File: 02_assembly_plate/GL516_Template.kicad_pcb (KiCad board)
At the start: 2 copper layers, 314.4 x 98.8 mm, 58 parts, among them J10 Conn_01x01, J11 Conn_01x01, J12 Conn_01x01, J13 Conn_01x01, J14 Conn_01x01, J15 Conn_01x01, J16 Conn_01x01, J17 Conn_01x01, J2 Conn_01x01, J3 Conn_01x01, J4 Conn_01x01, J5 Conn_01x01, J6 Conn_01x01, J7 Conn_01x01, J8 Conn_01x01, J9 Conn_01x01, SW1 KEY_SWITCH, SW10 KEY_SWITCH, SW11 KEY_SWITCH, SW12 KEY_SWITCH, SW13 KEY_SWITCH, SW14 KEY_SWITCH, SW15 KEY_SWITCH, SW16 KEY_SWITCH, SW17 KEY_SWITCH, SW18 KEY_SWITCH, SW19 KEY_SWITCH, SW2 KEY_SWITCH, SW20 KEY_SWITCH, SW21 KEY_SWITCH, SW22 KEY_SWITCH, SW23 KEY_SWITCH, SW24 KEY_SWITCH, SW25 KEY_SWITCH, SW26 KEY_SWITCH, SW27 KEY_SWITCH, SW28 KEY_SWITCH, SW29 KEY_SWITCH, SW3 KEY_SWITCH, SW30 KEY_SWITCH, SW31 KEY_SWITCH, SW32 KEY_SWITCH, SW33 KEY_SWITCH, SW34 KEY_SWITCH, SW35 KEY_SWITCH, SW36 KEY_SWITCH, SW37 KEY_SWITCH, SW38 KEY_SWITCH, SW39 KEY_SWITCH, SW4 KEY_SWITCH, SW40 KEY_SWITCH, SW41 KEY_SWITCH, SW42 KEY_SWITCH, SW5 KEY_SWITCH, SW6 KEY_SWITCH, SW7 KEY_SWITCH, SW8 KEY_SWITCH, SW9 KEY_SWITCH

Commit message: place all footprints and change edge.cuts
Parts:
- removed J10, J11, J12, J13, J14, J15, J16, J17, J8, J9: Conn_01x01, kbd_Hole:m2_Screw_Hole_Fab
- removed J2, J3, J4, J5, J6, J7: Conn_01x01, kbd_Hole:m2_Screw_Hole_EdgeCuts
- added D1: D, kbd_Parts:Diode_TH_SMD, F.Cu at (36.1, 53.3)
- added D10: D, kbd_Parts:Diode_TH_SMD, F.Cu at (93.3, 53.3)
- added D11: D, kbd_Parts:Diode_TH_SMD, F.Cu at (93.3, 72.3)
- added D12: D, kbd_Parts:Diode_TH_SMD, F.Cu at (93.3, 91.4)
- added D13: D, kbd_Parts:Diode_TH_SMD, F.Cu at (112.3, 53.3)
- added D14: D, kbd_Parts:Diode_TH_SMD, F.Cu at (112.3, 72.3)
- added D15: D, kbd_Parts:Diode_TH_SMD, F.Cu at (112.3, 91.4)
- added D16: D, kbd_Parts:Diode_TH_SMD, F.Cu at (112.3, 110.4)
- added D17: D, kbd_Parts:Diode_TH_SMD, F.Cu at (131.4, 53.3)
- added D18: D, kbd_Parts:Diode_TH_SMD, F.Cu at (131.4, 72.3)
- added D19: D, kbd_Parts:Diode_TH_SMD, F.Cu at (131.4, 91.4)
- added D2: D, kbd_Parts:Diode_TH_SMD, F.Cu at (36.1, 72.3)
- added D20: D, kbd_Parts:Diode_TH_SMD, F.Cu at (131.4, 110.4)
- added D21: D, kbd_Parts:Diode_TH_SMD, F.Cu at (150.4, 110.4)
- added D22: D, kbd_Parts:Diode_TH_SMD, F.Cu at (207.6, 110.4)
- added D23: D, kbd_Parts:Diode_TH_SMD, F.Cu at (226.6, 53.3)
- added D24: D, kbd_Parts:Diode_TH_SMD, F.Cu at (226.6, 72.3)
- added D25: D, kbd_Parts:Diode_TH_SMD, F.Cu at (226.6, 91.4)
- added D26: D, kbd_Parts:Diode_TH_SMD, F.Cu at (226.6, 110.4)
- added D27: D, kbd_Parts:Diode_TH_SMD, F.Cu at (245.7, 53.3)
- added D28: D, kbd_Parts:Diode_TH_SMD, F.Cu at (245.7, 72.3)
- added D29: D, kbd_Parts:Diode_TH_SMD, F.Cu at (245.7, 91.4)
- added D3: D, kbd_Parts:Diode_TH_SMD, F.Cu at (36.1, 91.4)
- added D30: D, kbd_Parts:Diode_TH_SMD, F.Cu at (245.7, 110.4)
- added D31: D, kbd_Parts:Diode_TH_SMD, F.Cu at (264.7, 53.3)
- added D32: D, kbd_Parts:Diode_TH_SMD, F.Cu at (264.7, 72.3)
- added D33: D, kbd_Parts:Diode_TH_SMD, F.Cu at (264.7, 91.4)
- added D34: D, kbd_Parts:Diode_TH_SMD, F.Cu at (283.8, 53.3)
- added D35: D, kbd_Parts:Diode_TH_SMD, F.Cu at (283.8, 72.3)
- added D36: D, kbd_Parts:Diode_TH_SMD, F.Cu at (283.8, 91.4)
- added D37: D, kbd_Parts:Diode_TH_SMD, F.Cu at (302.8, 53.3)
- added D38: D, kbd_Parts:Diode_TH_SMD, F.Cu at (302.8, 72.3)
- added D39: D, kbd_Parts:Diode_TH_SMD, F.Cu at (302.8, 91.4)
- added D4: D, kbd_Parts:Diode_TH_SMD, F.Cu at (55.2, 53.3)
- added D40: D, kbd_Parts:Diode_TH_SMD, F.Cu at (321.9, 53.3)
- added D41: D, kbd_Parts:Diode_TH_SMD, F.Cu at (321.9, 72.3)
- added D42: D, kbd_Parts:Diode_TH_SMD, F.Cu at (321.9, 91.4)
- added D5: D, kbd_Parts:Diode_TH_SMD, F.Cu at (55.2, 72.3)
- added D6: D, kbd_Parts:Diode_TH_SMD, F.Cu at (55.2, 91.4)
- added D7: D, kbd_Parts:Diode_TH_SMD, F.Cu at (74.2, 53.3)
- added D8: D, kbd_Parts:Diode_TH_SMD, F.Cu at (74.2, 72.3)
- added D9: D, kbd_Parts:Diode_TH_SMD, F.Cu at (74.2, 91.4)
- added J1: Conn_01x02, kbd_Parts:Battery_XH2.5_GL_PCB, F.Cu at (254.9, 23.8)
- added SW43: SW_PUSH, kbd_Parts:ResetSW, F.Cu at (271.4, 21.4)
- added U1: BLEMicroPro, kbd_Parts:Micon_BMP_GL, B.Cu at (301.6, 28.5)
- SW1, SW10, SW11, SW12, SW13, SW14, SW15, SW16, SW17, SW18, SW19, SW2, SW20, SW21, SW22, SW23, SW24, SW25, SW26, SW27, SW28, SW29, SW3, SW30, SW31, SW32, SW33, SW34, SW35, SW36, SW37, SW38, SW39, SW4, SW40, SW41, SW42, SW5, SW6, SW7, SW8, SW9: value KEY_SWITCH -> SW_PUSH; footprint kbd_SW_Hole:SW_Hole_1 -> kbd_SW:CherryMX_Hotswap_1.0u
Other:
- board size 314.4 x 98.8 mm -> 304.4 x 98.8 mm
- board text removed: "Put the ProMicro between here and there."

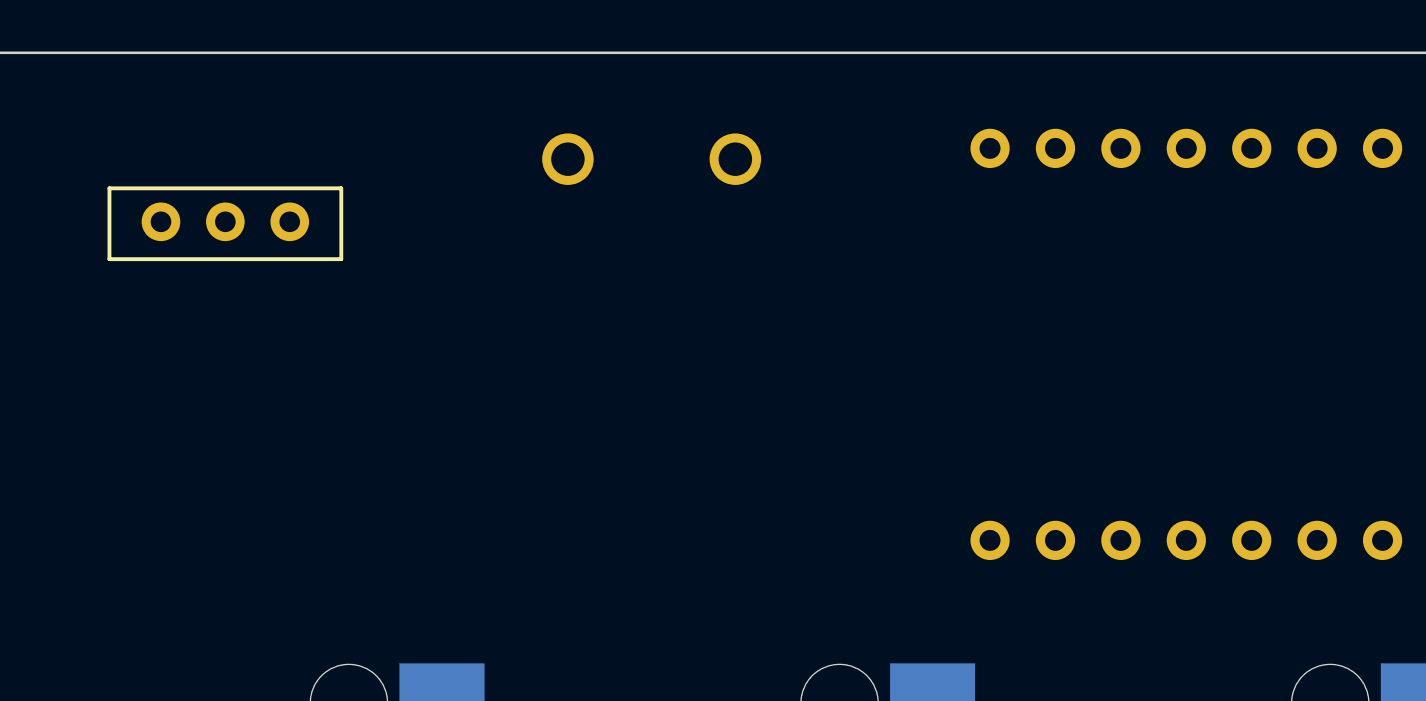
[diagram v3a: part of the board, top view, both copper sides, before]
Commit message: Wire GND, RST, BAT+
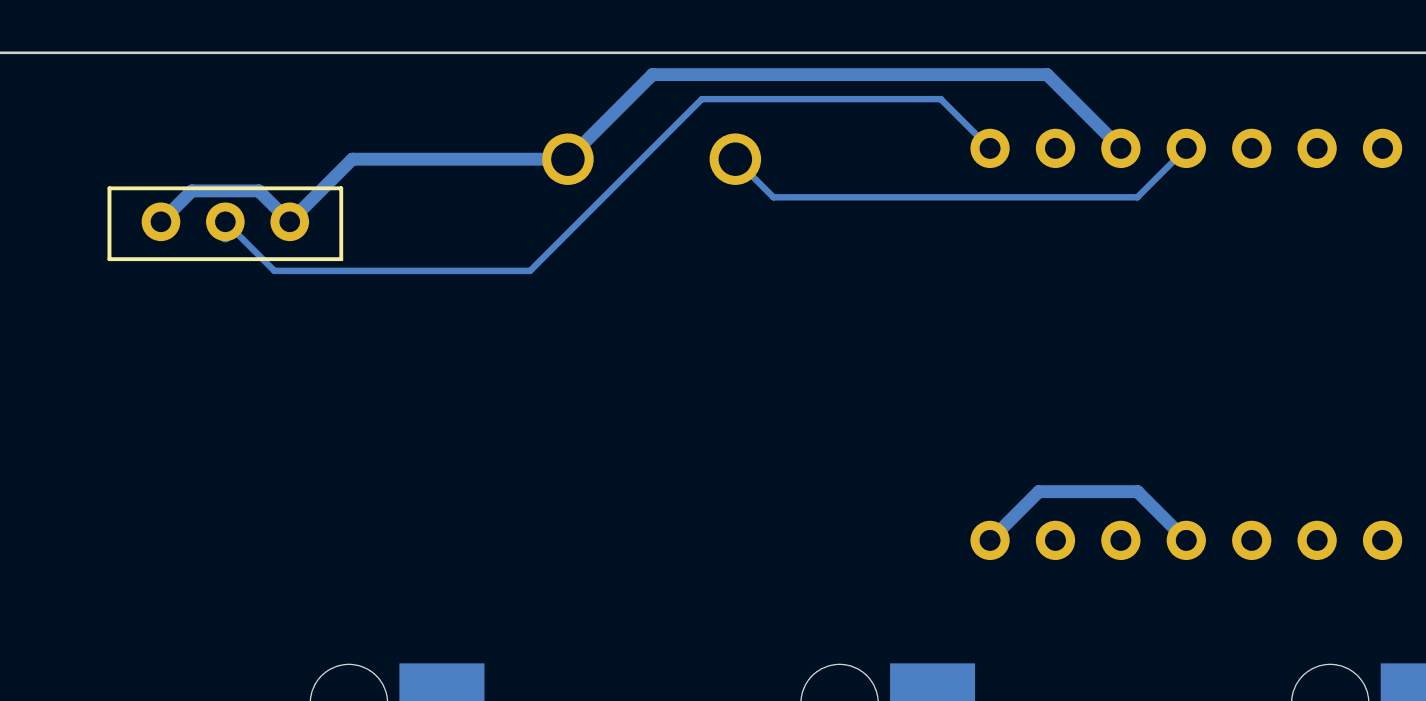
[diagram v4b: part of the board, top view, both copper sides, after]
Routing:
- net GND: track 0.00 -> 51.2 mm
- net Bat+: track 0.00 -> 34.8 mm
- net Reset: track 0.00 -> 18.9 mm
- net VCC: track 0.00 -> 0.53 mm
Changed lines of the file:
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@@
     (thickness 1.6)
     (drawings 701)
-    (tracks 0)
+    (tracks 24)
     (zones 0)
     (modules 87)
@@
     (38 B.Mask user)
     (39 F.Mask user)
-    (40 Dwgs.User user)
+    (40 Dwgs.User user hide)
     (41 Cmts.User user)
     (42 Eco1.User user)
@@
     (solder_mask_min_width 0.25)
     (aux_axis_origin 0 0)
-    (grid_origin 28.525 47.575)
     (visible_elements 7FFFFFFF)
     (pcbplotparams
@@
       (effects (font (size 0.75 0.5) (thickness 0.125)) (justify mirror))
     )
-    (fp_text user LED (at 5.5 14.478 270) (layer B.SilkS)
+    (fp_text user " " (at 5.5 14.478 270) (layer B.SilkS)
       (effects (font (size 0.75 0.5) (thickness 0.125)) (justify mirror))
     )
@@
   (gr_line (start 22.275 116.05) (end 320.625 116.05) (layer Edge.Cuts) (width 0.1))
   (gr_line (start 320.625 17.25) (end 22.275 17.25) (layer Edge.Cuts) (width 0.1))
+  (segment (start 259.7985 21.3807) (end 257.3672 23.812) (width 0.5) (layer B.Cu) (net 47))
+  (segment (start 268.1676 21.3807) (end 259.7985 21.3807) (width 0.5) (layer B.Cu) (net 47))
+  (segment (start 253.567201 22.611999) (end 252.3672 23.812) (width 0.5) (layer B.Cu) (net 47))
+  (segment (start 256.167199 22.611999) (end 253.567201 22.611999) (width 0.5) (layer B.Cu) (net 47))
+  (segment (start 257.3672 23.812) (end 256.167199 22.611999) (width 0.5) (layer B.Cu) (net 47))
+  (segment (start 284.7839 36.1814) (end 284.557 36.1814) (width 0.5) (layer B.Cu) (net 47))
+  (segment (start 290.2856 34.29) (end 292.177 36.1814) (width 0.5) (layer B.Cu) (net 47))
+  (segment (start 286.4484 34.29) (end 290.2856 34.29) (width 0.5) (layer B.Cu) (net 47))
+  (segment (start 284.557 36.1814) (end 286.4484 34.29) (width 0.5) (layer B.Cu) (net 47))
+  (segment (start 271.4508 18.0975) (end 268.1676 21.3807) (width 0.5) (layer B.Cu) (net 47))
+  (segment (start 286.7731 18.0975) (end 271.4508 18.0975) (width 0.5) (layer B.Cu) (net 47))
+  (segment (start 289.637 20.9614) (end 286.7731 18.0975) (width 0.5) (layer B.Cu) (net 47))
+  (segment (start 254.8672 24.3622) (end 254.8672 23.812) (width 0.5) (layer B.Cu) (net 48))
+  (segment (start 284.7911 20.9614) (end 284.557 20.9614) (width 0.5) (layer B.Cu) (net 48))
+  (segment (start 266.7 25.7175) (end 256.7727 25.7175) (width 0.25) (layer B.Cu) (net 48))
+  (segment (start 273.3675 19.05) (end 266.7 25.7175) (width 0.25) (layer B.Cu) (net 48))
+  (segment (start 256.7727 25.7175) (end 254.8672 23.812) (width 0.25) (layer B.Cu) (net 48))
+  (segment (start 282.6456 19.05) (end 273.3675 19.05) (width 0.25) (layer B.Cu) (net 48))
+  (segment (start 284.557 20.9614) (end 282.6456 19.05) (width 0.25) (layer B.Cu) (net 48))
+  (segment (start 276.1469 22.86) (end 274.6676 21.3807) (width 0.25) (layer B.Cu) (net 56))
+  (segment (start 290.2784 22.86) (end 276.1469 22.86) (width 0.25) (layer B.Cu) (net 56))
+  (segment (start 292.177 20.9614) (end 290.2784 22.86) (width 0.25) (layer B.Cu) (net 56))
+  (segment (start 294.717 20.9614) (end 295.1686 20.9614) (width 0.5) (layer B.Cu) (net 64))
+  (segment (start 295.1686 20.9614) (end 295.225 20.905) (width 0.5) (layer B.Cu) (net 64))
 )

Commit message: Wire Diode's PAT and Pin Hole
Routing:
- net Row0: track 0.00 -> 24.5 mm
- net Row2: track 0.00 -> 24.4 mm
- net Row1: track 0.00 -> 22.4 mm
- net Row3: track 0.00 -> 12.3 mm
- net Net-(D30-Pad1): track 0.00 -> 2.04 mm
- net Net-(D26-Pad1): track 0.00 -> 2.04 mm
- net Net-(D22-Pad1): track 0.00 -> 2.04 mm
- net Net-(D21-Pad2): track 0.00 -> 2.04 mm
- net Net-(D20-Pad2): track 0.00 -> 2.04 mm
- net Net-(D16-Pad2): track 0.00 -> 2.04 mm
- net Net-(D7-Pad2): track 0.00 -> 2.04 mm
- net Net-(D40-Pad1): track 0.00 -> 2.04 mm
- net Net-(D4-Pad2): track 0.00 -> 2.04 mm
- net Net-(D37-Pad1): track 0.00 -> 2.04 mm
- net Net-(D34-Pad1): track 0.00 -> 2.04 mm
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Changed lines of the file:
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@@
     (thickness 1.6)
     (drawings 701)
-    (tracks 24)
+    (tracks 110)
     (zones 0)
     (modules 87)
@@
   (page A3)
   (layers
-    (0 F.Cu signal)
+    (0 F.Cu signal hide)
     (31 B.Cu signal)
-    (32 B.Adhes user)
-    (33 F.Adhes user)
+    (32 B.Adhes user hide)
+    (33 F.Adhes user hide)
     (34 B.Paste user)
-    (35 F.Paste user)
-    (36 B.SilkS user)
-    (37 F.SilkS user)
+    (35 F.Paste user hide)
+    (36 B.SilkS user hide)
+    (37 F.SilkS user hide)
     (38 B.Mask user)
-    (39 F.Mask user)
+    (39 F.Mask user hide)
     (40 Dwgs.User user hide)
-    (41 Cmts.User user)
-    (42 Eco1.User user)
-    (43 Eco2.User user)
+    (41 Cmts.User user hide)
+    (42 Eco1.User user hide)
+    (43 Eco2.User user hide)
     (44 Edge.Cuts user)
-    (45 Margin user)
+    (45 Margin user hide)
     (46 B.CrtYd user)
-    (47 F.CrtYd user)
+    (47 F.CrtYd user hide)
     (48 B.Fab user)
-    (49 F.Fab user)
+    (49 F.Fab user hide)
   )
   (setup
@@
     (solder_mask_min_width 0.25)
     (aux_axis_origin 0 0)
-    (visible_elements 7FFFFFFF)
+    (visible_elements 7FFFF7FF)
     (pcbplotparams
       (layerselection 0x01000_7ffffffe)
@@
   (gr_line (start 22.275 116.05) (end 320.625 116.05) (layer Edge.Cuts) (width 0.1))
   (gr_line (start 320.625 17.25) (end 22.275 17.25) (layer Edge.Cuts) (width 0.1))
+  (segment (start 36.145 49.48) (end 36.145 51.515) (width 0.25) (layer B.Cu) (net 1))
+  (segment (start 297.1936 36.1814) (end 297.257 36.1814) (width 0.25) (layer B.Cu) (net 2))
+  (segment (start 321.895 55.065) (end 321.895 57.1) (width 0.25) (layer B.Cu) (net 2))
+  (segment (start 302.845 55.065) (end 302.845 57.1) (width 0.25) (layer B.Cu) (net 2))
+  (segment (start 283.795 55.065) (end 283.795 57.1) (width 0.25) (layer B.Cu) (net 2))
+  (segment (start 264.745 55.065) (end 264.745 57.1) (width 0.25) (layer B.Cu) (net 2))
+  (segment (start 245.695 55.065) (end 245.695 57.1) (width 0.25) (layer B.Cu) (net 2))
+  (segment (start 226.645 55.065) (end 226.645 57.1) (width 0.25) (layer B.Cu) (net 2))
+  (segment (start 131.395 55.065) (end 131.395 57.1) (width 0.25) (layer B.Cu) (net 2))
+  (segment (start 112.345 55.065) (end 112.345 57.1) (width 0.25) (layer B.Cu) (net 2))
+  (segment (start 93.295 55.065) (end 93.295 57.1) (width 0.25) (layer B.Cu) (net 2))
+  (segment (start 74.245 55.065) (end 74.245 57.1) (width 0.25) (layer B.Cu) (net 2))
+  (segment (start 55.195 55.065) (end 55.195 57.1) (width 0.25) (layer B.Cu) (net 2))
+  (segment (start 36.145 55.065) (end 36.145 57.1) (width 0.25) (layer B.Cu) (net 2))
+  (segment (start 36.145 68.53) (end 36.145 70.565) (width 0.25) (layer B.Cu) (net 3))
+  (segment (start 321.895 74.115) (end 321.895 76.15) (width 0.25) (layer B.Cu) (net 4))
+  (segment (start 302.845 74.115) (end 302.845 76.15) (width 0.25) (layer B.Cu) (net 4))
+  (segment (start 283.795 74.115) (end 283.795 76.15) (width 0.25) (layer B.Cu) (net 4))
+  (segment (start 264.745 74.115) (end 264.745 76.15) (width 0.25) (layer B.Cu) (net 4))
+  (segment (start 245.695 74.115) (end 245.695 76.15) (width 0.25) (layer B.Cu) (net 4))
+  (segment (start 131.395 74.115) (end 131.395 76.15) (width 0.25) (layer B.Cu) (net 4))
+  (segment (start 112.345 74.115) (end 112.345 76.15) (width 0.25) (layer B.Cu) (net 4))
+  (segment (start 93.295 74.115) (end 93.295 76.15) (width 0.25) (layer B.Cu) (net 4))
+  (segment (start 74.245 74.115) (end 74.245 76.15) (width 0.25) (layer B.Cu) (net 4))
+  (segment (start 55.195 74.115) (end 55.195 76.15) (width 0.25) (layer B.Cu) (net 4))
+  (segment (start 36.145 74.115) (end 36.145 76.15) (width 0.25) (layer B.Cu) (net 4))
+  (segment (start 36.145 87.58) (end 36.145 89.615) (width 0.25) (layer B.Cu) (net 5))
+  (segment (start 302.337 36.1814) (end 302.3506 36.195) (width 0.25) (layer B.Cu) (net 6))
+  (segment (start 321.895 93.165) (end 321.895 95.2) (width 0.25) (layer B.Cu) (net 6))
+  (segment (start 302.845 93.165) (end 302.845 95.2) (width 0.25) (layer B.Cu) (net 6))
+  (segment (start 283.795 93.165) (end 283.795 95.2) (width 0.25) (layer B.Cu) (net 6))
+  (segment (start 264.745 93.165) (end 264.745 95.2) (width 0.25) (layer B.Cu) (net 6))
+  (segment (start 245.695 93.165) (end 245.695 95.2) (width 0.25) (layer B.Cu) (net 6))
+  (segment (start 226.645 93.165) (end 226.645 95.2) (width 0.25) (layer B.Cu) (net 6))
+  (segment (start 131.395 93.165) (end 131.395 95.2) (width 0.25) (layer B.Cu) (net 6))
+  (segment (start 112.345 93.165) (end 112.345 95.2) (width 0.25) (layer B.Cu) (net 6))
+  (segment (start 93.295 93.165) (end 93.295 95.2) (width 0.25) (layer B.Cu) (net 6))
+  (segment (start 74.245 93.165) (end 74.245 95.2) (width 0.25) (layer B.Cu) (net 6))
+  (segment (start 55.195 93.165) (end 55.195 95.2) (width 0.25) (layer B.Cu) (net 6))
+  (segment (start 36.145 93.165) (end 36.145 95.2) (width 0.25) (layer B.Cu) (net 6))
+  (segment (start 55.195 49.48) (end 55.195 51.515) (width 0.25) (layer B.Cu) (net 7))
+  (segment (start 55.195 68.53) (end 55.195 70.565) (width 0.25) (layer B.Cu) (net 8))
+  (segment (start 55.195 87.58) (end 55.195 89.615) (width 0.25) (layer B.Cu) (net 9))
+  (segment (start 74.245 49.48) (end 74.245 51.515) (width 0.25) (layer B.Cu) (net 10))
+  (segment (start 74.245 68.53) (end 74.245 70.565) (width 0.25) (layer B.Cu) (net 11))
+  (segment (start 93.295 49.48) (end 93.295 51.515) (width 0.25) (layer B.Cu) (net 13))
+  (segment (start 93.295 68.53) (end 93.295 70.565) (width 0.25) (layer B.Cu) (net 14))
+  (segment (start 93.295 87.58) (end 93.295 89.615) (width 0.25) (layer B.Cu) (net 15))
+  (segment (start 112.345 49.48) (end 112.345 51.515) (width 0.25) (layer B.Cu) (net 16))
+  (segment (start 112.345 68.53) (end 112.345 70.565) (width 0.25) (layer B.Cu) (net 17))
+  (segment (start 112.345 87.58) (end 112.345 89.615) (width 0.25) (layer B.Cu) (net 18))
+  (segment (start 112.345 106.63) (end 112.345 108.665) (width 0.25) (layer B.Cu) (net 19))
+  (segment (start 304.8136 36.1814) (end 304.877 36.1814) (width 0.25) (layer B.Cu) (net 20))
+  (segment (start 245.695 112.215) (end 245.695 114.25) (width 0.25) (layer B.Cu) (net 20))
+  (segment (start 226.645 112.215) (end 226.645 114.25) (width 0.25) (layer B.Cu) (net 20))
+  (segment (start 207.595 112.215) (end 207.595 114.25) (width 0.25) (layer B.Cu) (net 20))
+  (segment (start 150.445 112.215) (end 150.445 114.25) (width 0.25) (layer B.Cu) (net 20))
+  (segment (start 131.395 112.215) (end 131.395 114.25) (width 0.25) (layer B.Cu) (net 20))
+  (segment (start 112.345 112.215) (end 112.345 114.25) (width 0.25) (layer B.Cu) (net 20))
+  (segment (start 131.395 49.48) (end 131.395 51.515) (width 0.25) (layer B.Cu) (net 21))
+  (segment (start 131.395 68.53) (end 131.395 70.565) (width 0.25) (layer B.Cu) (net 22))
+  (segment (start 131.395 87.58) (end 131.395 89.615) (width 0.25) (layer B.Cu) (net 23))
+  (segment (start 131.395 106.63) (end 131.395 108.665) (width 0.25) (layer B.Cu) (net 24))
+  (segment (start 150.445 106.63) (end 150.445 108.665) (width 0.25) (layer B.Cu) (net 25))
+  (segment (start 207.595 106.63) (end 207.595 108.665) (width 0.25) (layer B.Cu) (net 26))
+  (segment (start 226.645 49.48) (end 226.645 51.515) (width 0.25) (layer B.Cu) (net 27))
+  (segment (start 226.645 68.53) (end 226.645 70.565) (width 0.25) (layer B.Cu) (net 28))
+  (segment (start 226.645 87.58) (end 226.645 89.615) (width 0.25) (layer B.Cu) (net 29))
+  (segment (start 226.645 106.63) (end 226.645 108.665) (width 0.25) (layer B.Cu) (net 30))
+  (segment (start 245.695 49.48) (end 245.695 51.515) (width 0.25) (layer B.Cu) (net 31))
+  (segment (start 245.695 68.53) (end 245.695 70.565) (width 0.25) (layer B.Cu) (net 32))
+  (segment (start 245.695 87.58) (end 245.695 89.615) (width 0.25) (layer B.Cu) (net 33))
+  (segment (start 245.695 106.63) (end 245.695 108.665) (width 0.25) (layer B.Cu) (net 34))
+  (segment (start 264.745 49.48) (end 264.745 51.515) (width 0.25) (layer B.Cu) (net 35))
+  (segment (start 264.745 68.53) (end 264.745 70.565) (width 0.25) (layer B.Cu) (net 36))
+  (segment (start 264.745 87.58) (end 264.745 89.615) (width 0.25) (layer B.Cu) (net 37))
+  (segment (start 283.795 49.48) (end 283.795 51.515) (width 0.25) (layer B.Cu) (net 38))
+  (segment (start 283.795 68.53) (end 283.795 70.565) (width 0.25) (layer B.Cu) (net 39))
+  (segment (start 283.795 87.58) (end 283.795 89.615) (width 0.25) (layer B.Cu) (net 40))
+  (segment (start 302.845 49.48) (end 302.845 51.515) (width 0.25) (layer B.Cu) (net 41))
+  (segment (start 302.845 68.53) (end 302.845 70.565) (width 0.25) (layer B.Cu) (net 42))
+  (segment (start 302.845 87.58) (end 302.845 89.615) (width 0.25) (layer B.Cu) (net 43))
+  (segment (start 321.895 49.48) (end 321.895 51.515) (width 0.25) (layer B.Cu) (net 44))
+  (segment (start 321.895 68.53) (end 321.895 70.565) (width 0.25) (layer B.Cu) (net 45))
+  (segment (start 321.895 87.58) (end 321.895 89.615) (width 0.25) (layer B.Cu) (net 46))
   (segment (start 259.7985 21.3807) (end 257.3672 23.812) (width 0.5) (layer B.Cu) (net 47))
   (segment (start 268.1676 21.3807) (end 259.7985 21.3807) (width 0.5) (layer B.Cu) (net 47))
@@
   (segment (start 282.6456 19.05) (end 273.3675 19.05) (width 0.25) (layer B.Cu) (net 48))
   (segment (start 284.557 20.9614) (end 282.6456 19.05) (width 0.25) (layer B.Cu) (net 48))
+  (segment (start 312.4264 20.9614) (end 312.497 20.9614) (width 0.25) (layer B.Cu) (net 55))
   (segment (start 276.1469 22.86) (end 274.6676 21.3807) (width 0.25) (layer B.Cu) (net 56))
   (segment (start 290.2784 22.86) (end 276.1469 22.86) (width 0.25) (layer B.Cu) (net 56))

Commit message: Wire SW Socket's 2nd Pats and Diodes
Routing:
- net Net-(D2-Pad2): track 2.03 -> 9.90 mm
- net Net-(D38-Pad1): track 2.03 -> 9.86 mm
- net Net-(D35-Pad1): track 2.03 -> 9.86 mm
- net Net-(D32-Pad1): track 2.03 -> 9.86 mm
- net Net-(D24-Pad1): track 2.03 -> 9.86 mm
- net Net-(D18-Pad2): track 2.03 -> 9.86 mm
- net Net-(D37-Pad1): track 2.04 -> 9.86 mm
- net Net-(D34-Pad1): track 2.04 -> 9.86 mm
- net Net-(D31-Pad1): track 2.04 -> 9.86 mm
- net Net-(D23-Pad1): track 2.04 -> 9.86 mm
- net Net-(D17-Pad2): track 2.04 -> 9.86 mm
- net Net-(D39-Pad1): track 2.03 -> 9.86 mm
- net Net-(D36-Pad1): track 2.03 -> 9.86 mm
- net Net-(D33-Pad1): track 2.03 -> 9.86 mm
- net Net-(D25-Pad1): track 2.03 -> 9.86 mm
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
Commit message: Wire Col
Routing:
- net Col0: track 0.00 -> 409.8 mm
- net Col1: track 0.00 -> 389.0 mm, vias 0 -> 2
- net Col2: track 0.00 -> 371.0 mm, vias 0 -> 2
- net Col4: track 0.00 -> 335.4 mm, vias 0 -> 2
- net Col3: track 0.00 -> 334.2 mm, vias 0 -> 2
- net Col5: track 0.00 -> 333.2 mm, vias 0 -> 2
- net Col6: track 0.07 -> 282.9 mm, vias 0 -> 2
